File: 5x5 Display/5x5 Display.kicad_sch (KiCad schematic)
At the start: 46 parts, among them U3 DRV1

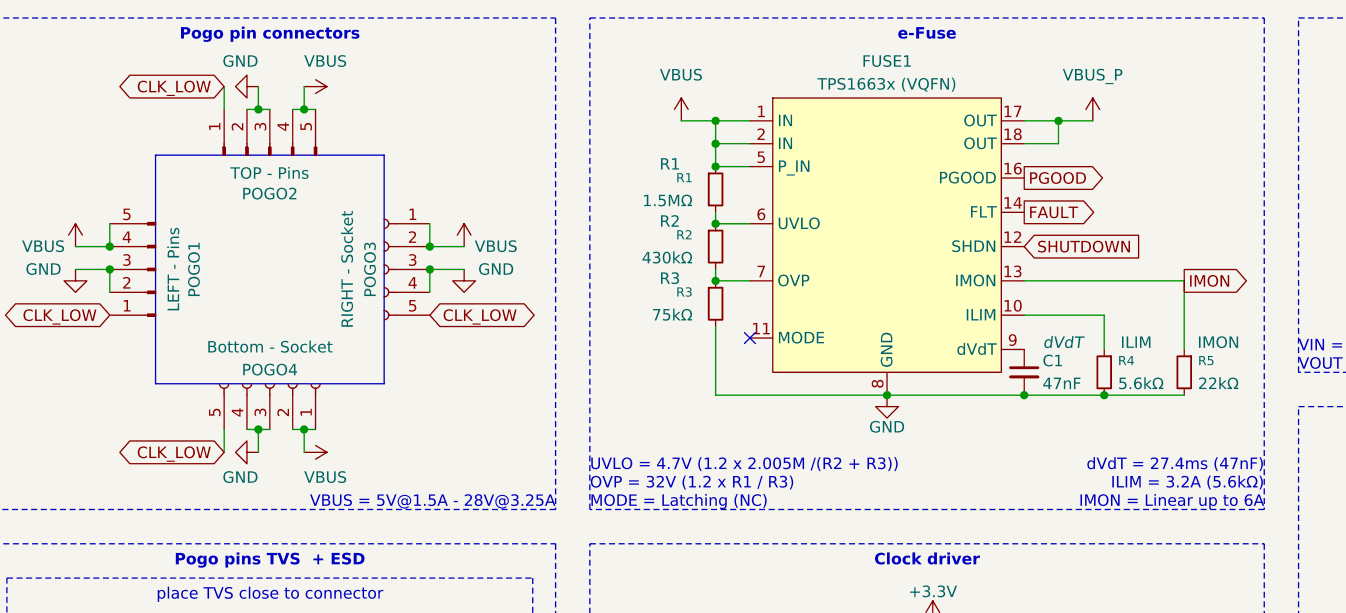
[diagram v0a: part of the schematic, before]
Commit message: Update schematic wiring and component positions
Adjusted wire routing and junctions around the 58.42mm y-coordinate, updated positions of R2 and R3, and changed some property values for clarity. These changes improve schematic readability and correct net connections in the 5x5 Display KiCad project.
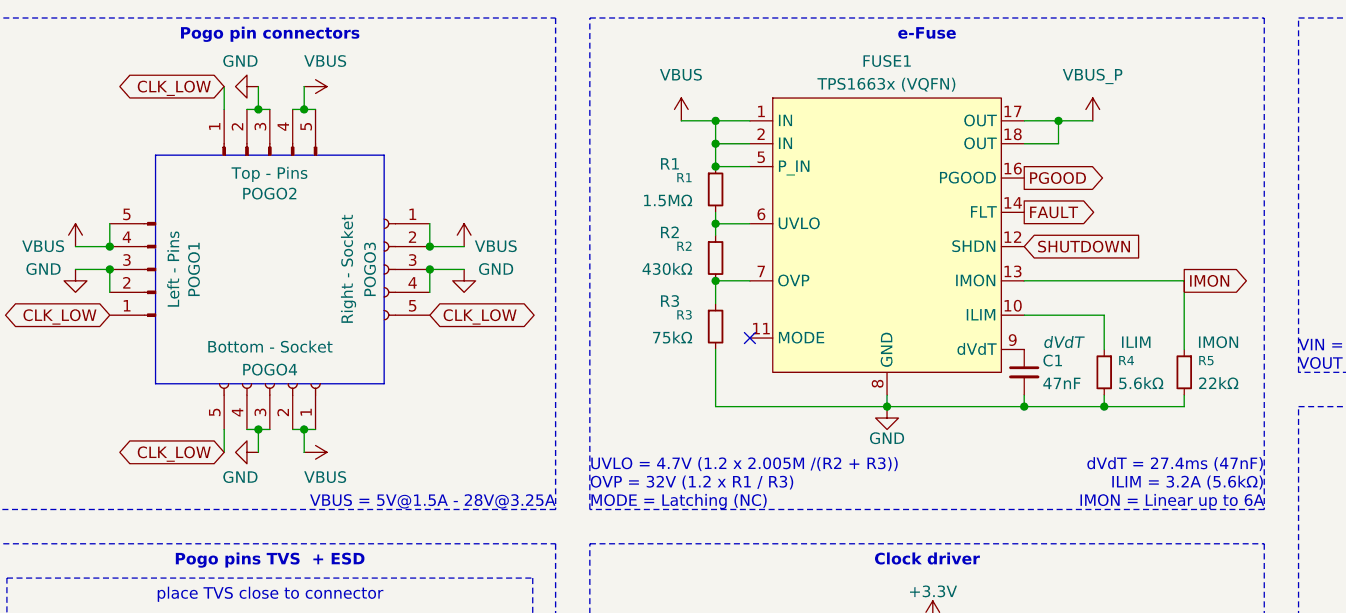
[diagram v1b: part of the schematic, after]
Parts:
- POGO1: value LEFT - Pins -> Left - Pins
- POGO2: value TOP - Pins -> Top - Pins
- POGO3: value RIGHT - Socket -> Right - Socket
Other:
- moved on the sheet: R2, R3
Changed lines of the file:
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@@
 	)
 	(junction
-		(at 250.19 100.33)
+		(at 130.81 58.42)
 		(diameter 0)
 		(color 0 0 0 0)
 	)
 	(junction
-		(at 218.44 80.01)
+		(at 250.19 100.33)
 		(diameter 0)
 		(color 0 0 0 0)
 	)
 	(junction
-		(at 208.28 74.93)
+		(at 218.44 80.01)
 		(diameter 0)
 		(color 0 0 0 0)
 	)
 	(junction
-		(at 96.52 38.1)
+		(at 208.28 74.93)
 		(diameter 0)
 		(color 0 0 0 0)
 	)
 	(junction
-		(at 139.7 57.15)
+		(at 96.52 38.1)
 		(diameter 0)
 		(color 0 0 0 0)
@@
 	)
 	(junction
-		(at 130.81 57.15)
+		(at 139.7 58.42)
 		(diameter 0)
 		(color 0 0 0 0)
@@
 	)
 	(junction
-		(at 115.57 57.15)
-		(diameter 0)
-		(color 0 0 0 0)
-	)
-	(junction
 		(at 171.45 69.85)
 		(diameter 0)
@@
 	)
 	(junction
+		(at 115.57 58.42)
+		(diameter 0)
+		(color 0 0 0 0)
+	)
+	(junction
 		(at 208.28 30.48)
 		(diameter 0)
@@
 	(wire
 		(pts
-			(xy 96.52 57.15) (xy 115.57 57.15)
+			(xy 96.52 46.99) (xy 96.52 44.45)
+		)
+		(stroke
+			(width 0)
+			(type default)
+		)
+	)
+	(wire
+		(pts
+			(xy 96.52 58.42) (xy 115.57 58.42)
 		)
 		(stroke
@@
 	(wire
 		(pts
+			(xy 96.52 39.37) (xy 96.52 38.1)
+		)
+		(stroke
+			(width 0)
+			(type default)
+		)
+	)
+	(wire
+		(pts
+			(xy 115.57 58.42) (xy 115.57 57.15)
+		)
+		(stroke
+			(width 0)
+			(type default)
+		)
+	)
+	(wire
+		(pts
 			(xy 64.77 40.64) (xy 64.77 38.1)
 		)
@@
 	(wire
 		(pts
-			(xy 115.57 57.15) (xy 130.81 57.15)
+			(xy 115.57 58.42) (xy 130.81 58.42)
 		)
 		(stroke
@@
 	(wire
 		(pts
+			(xy 139.7 58.42) (xy 139.7 57.15)
+		)
+		(stroke
+			(width 0)
+			(type default)
+		)
+	)
+	(wire
+		(pts
 			(xy 36.83 88.9) (xy 35.56 88.9)
 		)
@@
 	(wire
 		(pts
-			(xy 139.7 57.15) (xy 148.59 57.15)
+			(xy 139.7 58.42) (xy 148.59 58.42)
 		)
 		(stroke
@@
 	(wire
 		(pts
-			(xy 130.81 57.15) (xy 139.7 57.15)
+			(xy 130.81 58.42) (xy 139.7 58.42)
 		)
 		(stroke
@@
 	(wire
 		(pts
-			(xy 96.52 49.53) (xy 96.52 57.15)
-		)
-		(stroke
-			(width 0)
-			(type default)
-		)
-	)
-	(wire
-		(pts
-			(xy 96.52 43.18) (xy 96.52 44.45)
+			(xy 96.52 52.07) (xy 96.52 58.42)
 		)
 		(stroke
@@
 	(wire
 		(pts
+			(xy 130.81 58.42) (xy 130.81 57.15)
+		)
+		(stroke
+			(width 0)
+			(type default)
+		)
+	)
+	(wire
+		(pts
+			(xy 148.59 58.42) (xy 148.59 57.15)
+		)
+		(stroke
+			(width 0)
+			(type default)
+		)
+	)
+	(wire
+		(pts
 			(xy 96.52 36.83) (xy 96.52 38.1)
 		)
@@
 			)
 		)
-		(property "Value" "RIGHT - Socket"
+		(property "Value" "Right - Socket"
 			(at 55.626 43.18 90)
 			(effects
@@
 			)
 		)
-		(property "Value" "TOP - Pins"
+		(property "Value" "Top - Pins"
 			(at 46.99 32.512 90)
 			(effects
@@
 	(symbol
 		(lib_id "Device:R_Small")
-		(at 96.52 40.64 0)
+		(at 96.52 41.91 0)
 		(unit 1)
 		(exclude_from_sim no)
@@
 		(dnp no)
 		(property "Reference" "R2"
-			(at 93.98 39.3699 0)
+			(at 93.98 40.6399 0)
 			(effects
 				(font
@@
 		)
 		(property "Value" "430kΩ"
-			(at 93.98 41.9099 0)
+			(at 93.98 43.1799 0)
 			(effects
 				(font
@@
 		)
 		(property "Footprint" "Resistor_SMD:R_0603_1608Metric"
-			(at 96.52 40.64 0)
+			(at 96.52 41.91 0)
 			(effects
 				(font
@@
 		)
 		(property "Datasheet" "~"
-			(at 96.52 40.64 0)
+			(at 96.52 41.91 0)
 			(effects
 				(font
@@
 		)
 		(property "Description" "Resistor, small symbol"
-			(at 96.52 40.64 0)
+			(at 96.52 41.91 0)
 			(effects
 				(font
@@
 		)
 		(property "LCSC Part #" ""
-			(at 96.52 40.64 0)
+			(at 96.52 41.91 0)
 			(effects
 				(font
@@
 		)
 		(property "Name" "R2"
-			(at 91.44 37.846 0)
+			(at 91.44 39.116 0)
 			(effects
 				(font
@@
 	(symbol
 		(lib_id "power:GND")
-		(at 115.57 57.15 0)
+		(at 115.57 58.42 0)
 		(unit 1)
 		(exclude_from_sim no)
@@
 		(dnp no)
 		(property "Reference" "#PWR0161"
-			(at 115.57 63.5 0)
+			(at 115.57 64.77 0)
 			(effects
 				(font
@@
 		)
 		(property "Value" "GND"
-			(at 115.57 60.706 0)
+			(at 115.57 61.976 0)
 			(effects
 				(font
@@
 		)
 		(property "Footprint" ""
-			(at 115.57 57.15 0)
+			(at 115.57 58.42 0)
 			(effects
 				(font
@@
 		)
 		(property "Datasheet" ""
-			(at 115.57 57.15 0)
+			(at 115.57 58.42 0)
 			(effects
 				(font
@@
 		)
 		(property "Description" "Power symbol creates a global label with name \"GND\" , ground"
-			(at 115.57 57.15 0)
+			(at 115.57 58.42 0)
 			(effects
 				(font
@@
 	(symbol
 		(lib_id "Device:R_Small")
-		(at 96.52 46.99 0)
+		(at 96.52 49.53 0)
 		(unit 1)
 		(exclude_from_sim no)
@@
 		(dnp no)
 		(property "Reference" "R3"
-			(at 93.98 45.7199 0)
+			(at 93.98 48.2599 0)
 			(effects
 				(font
@@
 		)
 		(property "Value" "75kΩ"
-			(at 93.98 48.2599 0)
+			(at 93.98 50.7999 0)
 			(effects
 				(font
@@
 		)
 		(property "Footprint" "Resistor_SMD:R_0603_1608Metric"
-			(at 96.52 46.99 0)
+			(at 96.52 49.53 0)
 			(effects
 				(font
@@
 		)
 		(property "Datasheet" "~"
-			(at 96.52 46.99 0)
+			(at 96.52 49.53 0)
 			(effects
 				(font
@@
 		)
 		(property "Description" "Resistor, small symbol"
-			(at 96.52 46.99 0)
+			(at 96.52 49.53 0)
 			(effects
 				(font
@@
 		)
 		(property "LCSC Part #" ""
-			(at 96.52 46.99 0)
+			(at 96.52 49.53 0)
 			(effects
 				(font
@@
 		)
 		(property "Name" "R3"
-			(at 91.44 44.196 0)
+			(at 91.44 46.736 0)
 			(effects
 				(font
@@
 			)
 		)
-		(property "Value" "LEFT - Pins"
+		(property "Value" "Left - Pins"
 			(at 36.322 43.18 90)
 			(effects

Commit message: Footprint assignment finished
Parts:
- D10: footprint (none) -> Diode_SMD:D_SOD-323
- D6, D7, D8, D9: footprint (none) -> Diode_SMD:D_SMA
- L1, L2: footprint (none) -> Inductor_SMD:L_6.3x6.3_H3
- NT1, NT2: footprint (none) -> NetTie:NetTie-2_THT_Pad1.0mm
- POGO1, POGO2, POGO3, POGO4: footprint (none) -> Connector_PinSocket_2.54mm:PinSocket_1x05_P2.54mm_Horizontal
- REG1, REG2: footprint (none) -> TPS56637:TPS56637 VQFN-HR (10)
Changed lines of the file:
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@@
 			)
 		)
-		(property "Footprint" ""
+		(property "Footprint" "NetTie:NetTie-2_THT_Pad1.0mm"
 			(at 196.85 45.72 0)
 			(effects
@@
 			)
 		)
-		(property "Footprint" ""
+		(property "Footprint" "Diode_SMD:D_SMA"
 			(at 60.96 104.14 0)
 			(effects
@@
 			)
 		)
-		(property "Footprint" ""
+		(property "Footprint" "Diode_SMD:D_SMA"
 			(at 60.96 88.9 0)
 			(effects
@@
 			)
 		)
-		(property "Footprint" ""
+		(property "Footprint" "TPS56637:TPS56637 VQFN-HR (10)"
 			(at 195.58 76.2 0)
 			(effects
@@
 			)
 		)
-		(property "Footprint" ""
+		(property "Footprint" "TPS56637:TPS56637 VQFN-HR (10)"
 			(at 195.58 31.75 0)
 			(effects
@@
 			)
 		)
-		(property "Footprint" ""
+		(property "Footprint" "Connector_PinSocket_2.54mm:PinSocket_1x05_P2.54mm_Horizontal"
 			(at 59.69 43.18 0)
 			(effects
@@
 			)
 		)
-		(property "Footprint" ""
+		(property "Footprint" "Connector_PinSocket_2.54mm:PinSocket_1x05_P2.54mm_Horizontal"
 			(at 46.99 30.48 0)
 			(effects
@@
 			)
 		)
-		(property "Footprint" ""
+		(property "Footprint" "NetTie:NetTie-2_THT_Pad1.0mm"
 			(at 196.85 90.17 0)
 			(effects
@@
 			)
 		)
-		(property "Footprint" ""
+		(property "Footprint" "Diode_SMD:D_SOD-323"
 			(at 48.26 120.65 0)
 			(effects
@@
 			)
 		)
-		(property "Footprint" ""
+		(property "Footprint" "Diode_SMD:D_SMA"
 			(at 33.02 104.14 0)
 			(effects
@@
 			)
 		)
-		(property "Footprint" ""
+		(property "Footprint" "Connector_PinSocket_2.54mm:PinSocket_1x05_P2.54mm_Horizontal"
 			(at 46.99 55.88 0)
 			(effects
@@
 			)
 		)
-		(property "Footprint" ""
+		(property "Footprint" "Inductor_SMD:L_6.3x6.3_H3"
 			(at 212.09 74.93 0)
 			(effects
@@
 			)
 		)
-		(property "Footprint" ""
+		(property "Footprint" "Diode_SMD:D_SMA"
 			(at 33.02 88.9 0)
 			(effects
@@
 			)
 		)
-		(property "Footprint" ""
+		(property "Footprint" "Connector_PinSocket_2.54mm:PinSocket_1x05_P2.54mm_Horizontal"
 			(at 34.29 43.18 0)
 			(effects
@@
 			)
 		)
-		(property "Footprint" ""
+		(property "Footprint" "Inductor_SMD:L_6.3x6.3_H3"
 			(at 212.09 30.48 0)
 			(effects

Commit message: Add test points to schematic
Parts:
- added TP1: VBUS, symbol Connector:TestPoint
- added TP10, TP11, TP12: GND, symbol Connector:TestPoint
- added TP2: VBUS_P, symbol Connector:TestPoint
- added TP3: CLK_LOW, symbol Connector:TestPoint
- added TP4: CLK, symbol Connector:TestPoint
- added TP5: PGOOD, symbol Connector:TestPoint
- added TP6: +3.3v, symbol Connector:TestPoint
- added TP7: +5v, symbol Connector:TestPoint
- added TP8: LED LDO, symbol Connector:TestPoint
- added TP9: AGND, symbol Connector:TestPoint
- C1, C3, C6, C8, C9: footprint Capacitor_SMD:C_0805_2012Metric -> Capacitor_SMD:C_0603_1608Metric
- D10: now not fitted
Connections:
- net PGND is gone; now on net GND: C2.2, C5.2
- net +3.3V: now also TP6.1
- net +5V: now also TP7.1
- net +5V LED: now also TP8.1
- net AGND: now also TP9.1
- net CLK: now also TP4.1
- net CLK_LOW: now also TP3.1
- net GND: now also TP10.1, TP11.1, TP12.1
- net PGOOD: now also TP5.1
- net VBUS: now also TP1.1
- net VBUS_P: now also TP2.1
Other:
- note removed: "place TVS as close to connector as possible"
- moved on the sheet: D6, D7, D8, D9

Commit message: Assign test point footprints in schematic
Set the 'Footprint' property to 'TestPoint:TestPoint_Pad_D1.5mm' for multiple components in the 5x5 Display schematic. This change ensures correct footprint assignment for test points in PCB layout.
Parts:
- TP1, TP10, TP11, TP12, TP2, TP3, TP4, TP5, TP6, TP7, TP8, TP9: footprint (none) -> TestPoint:TestPoint_Pad_D1.5mm
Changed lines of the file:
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@@
 			)
 		)
-		(property "Footprint" ""
+		(property "Footprint" "TestPoint:TestPoint_Pad_D1.5mm"
 			(at 194.31 148.59 0)
 			(effects
@@
 			)
 		)
-		(property "Footprint" ""
+		(property "Footprint" "TestPoint:TestPoint_Pad_D1.5mm"
 			(at 167.64 148.59 0)
 			(effects
@@
 			)
 		)
-		(property "Footprint" ""
+		(property "Footprint" "TestPoint:TestPoint_Pad_D1.5mm"
 			(at 229.87 148.59 0)
 			(effects
@@
 			)
 		)
-		(property "Footprint" ""
+		(property "Footprint" "TestPoint:TestPoint_Pad_D1.5mm"
 			(at 265.43 148.59 0)
 			(effects
@@
 			)
 		)
-		(property "Footprint" ""
+		(property "Footprint" "TestPoint:TestPoint_Pad_D1.5mm"
 			(at 203.2 148.59 0)
 			(effects
@@
 			)
 		)
-		(property "Footprint" ""
+		(property "Footprint" "TestPoint:TestPoint_Pad_D1.5mm"
 			(at 185.42 148.59 0)
 			(effects
@@
 			)
 		)
-		(property "Footprint" ""
+		(property "Footprint" "TestPoint:TestPoint_Pad_D1.5mm"
 			(at 220.98 148.59 0)
 			(effects
@@
 			)
 		)
-		(property "Footprint" ""
+		(property "Footprint" "TestPoint:TestPoint_Pad_D1.5mm"
 			(at 238.76 148.59 0)
 			(effects
@@
 			)
 		)
-		(property "Footprint" ""
+		(property "Footprint" "TestPoint:TestPoint_Pad_D1.5mm"
 			(at 212.09 148.59 0)
 			(effects
@@
 			)
 		)
-		(property "Footprint" ""
+		(property "Footprint" "TestPoint:TestPoint_Pad_D1.5mm"
 			(at 247.65 148.59 0)
 			(effects
@@
 			)
 		)
-		(property "Footprint" ""
+		(property "Footprint" "TestPoint:TestPoint_Pad_D1.5mm"
 			(at 256.54 148.59 0)
 			(effects
@@
 			)
 		)
-		(property "Footprint" ""
+		(property "Footprint" "TestPoint:TestPoint_Pad_D1.5mm"
 			(at 176.53 148.59 0)
 			(effects

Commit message: buck layout
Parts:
- NT1, NT2: footprint NetTie:NetTie-2_THT_Pad1.0mm -> NetTie:NetTie-2_SMD_Pad0.5mm
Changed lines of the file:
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@@
 			)
 		)
-		(property "Footprint" "NetTie:NetTie-2_THT_Pad1.0mm"
+		(property "Footprint" "NetTie:NetTie-2_SMD_Pad0.5mm"
 			(at 196.85 45.72 0)
 			(effects
@@
 			)
 		)
-		(property "Footprint" "NetTie:NetTie-2_THT_Pad1.0mm"
+		(property "Footprint" "NetTie:NetTie-2_SMD_Pad0.5mm"
 			(at 196.85 90.17 0)
 			(effects

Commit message: Initial route complete
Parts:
- removed TP10, TP11: GND, TestPoint:TestPoint_Pad_D1.5mm, symbol Connector:TestPoint
- removed TP2: VBUS_P, TestPoint:TestPoint_Pad_D1.5mm, symbol Connector:TestPoint
- removed TP4: CLK, TestPoint:TestPoint_Pad_D1.5mm, symbol Connector:TestPoint
- removed TP5: PGOOD, TestPoint:TestPoint_Pad_D1.5mm, symbol Connector:TestPoint
- removed TP9: AGND, TestPoint:TestPoint_Pad_D1.5mm, symbol Connector:TestPoint
- D10: now left out of the parts list
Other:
- moved on the sheet: TP1, TP12, TP3, TP6, TP7, TP8

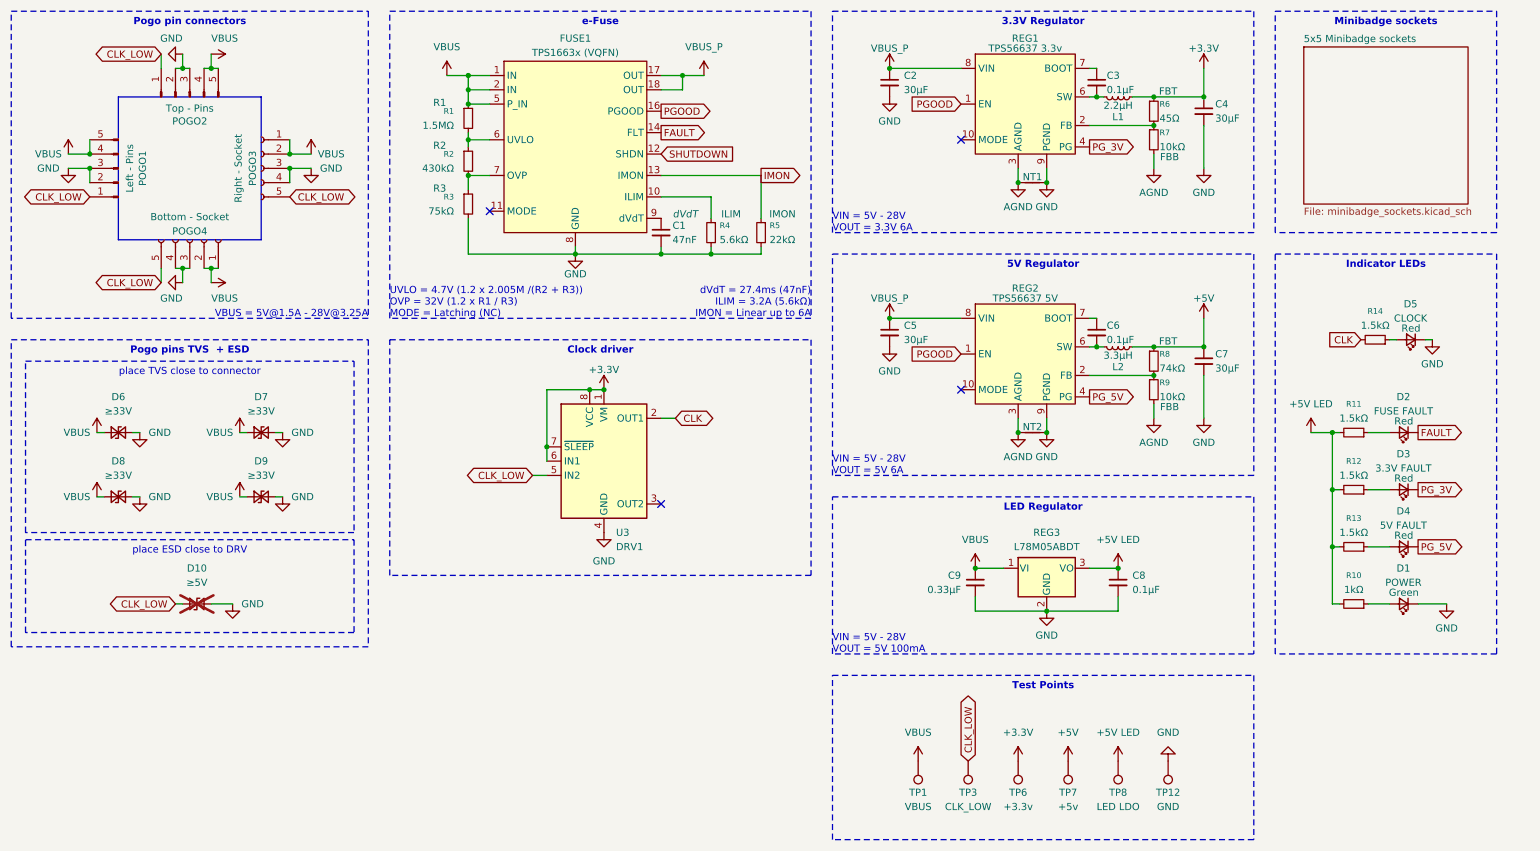
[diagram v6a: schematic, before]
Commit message: Silkscreens and components
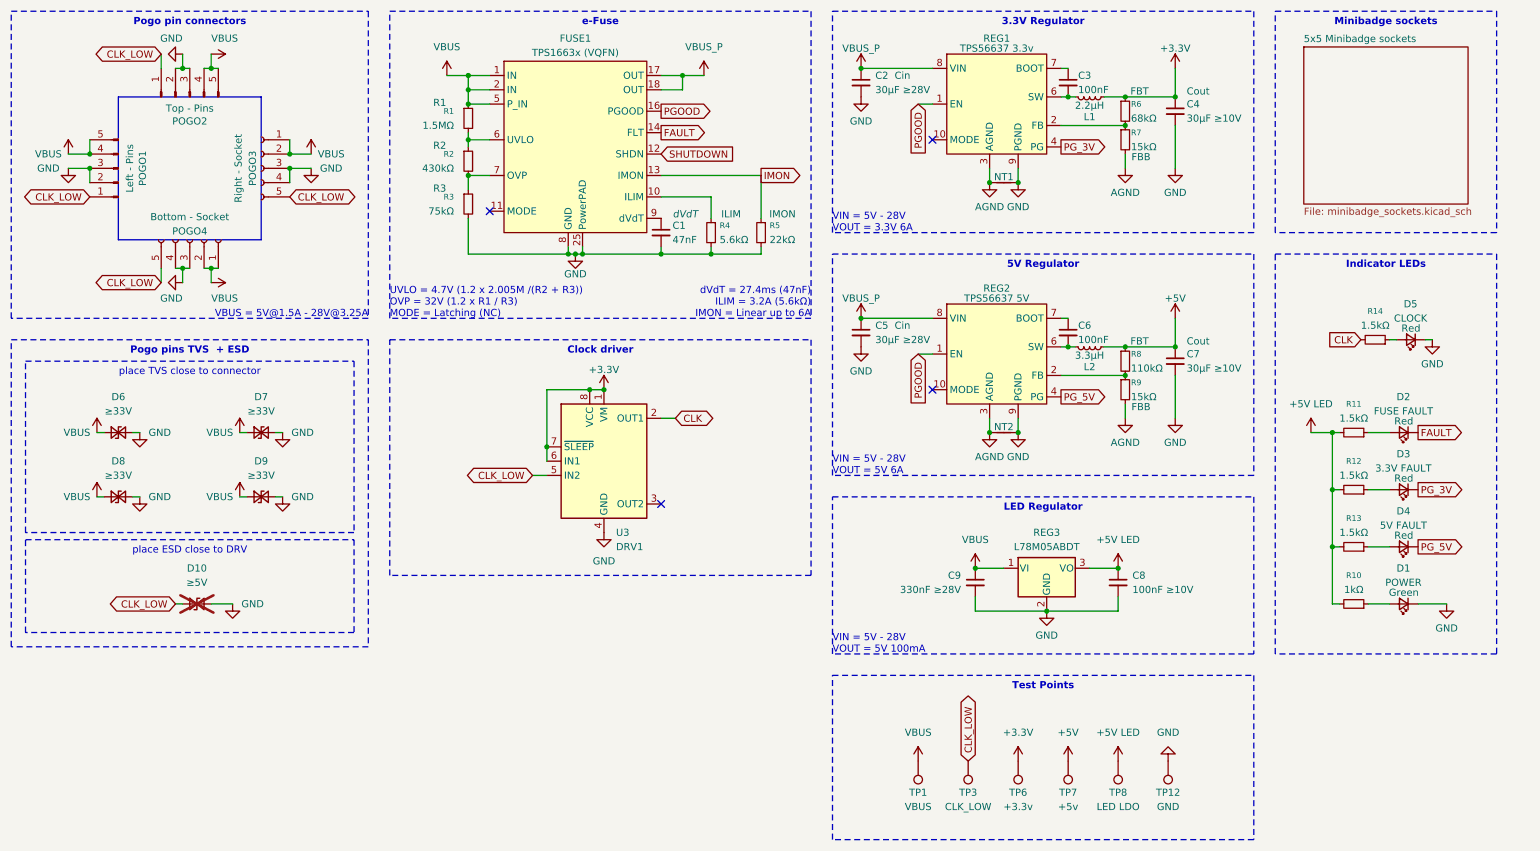
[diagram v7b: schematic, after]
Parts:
- C1: LCSC Part # (none) -> C1622
- C2, C5: value 30μF -> 30μF ≥28V; Name (none) -> Cin
- C3, C6: value 0.1μF -> 100nF; LCSC Part # (none) -> C14663
- C4, C7: value 30μF -> 30μF ≥10V; LCSC Part # (none) -> C96123; Name (none) -> Cout
- C8: value 0.1μF -> 100nF ≥10V; LCSC Part # (none) -> C14663
- C9: value 0.33μF -> 330nF ≥28V; footprint Capacitor_SMD:C_0603_1608Metric -> Capacitor_SMD:C_0805_2012Metric; LCSC Part # (none) -> C1740
- D1: LCSC Part # (none) -> C2297
- D2, D3, D4, D5: LCSC Part # (none) -> C84256
- R1: LCSC Part # (none) -> C4172
- R10: LCSC Part # (none) -> C21190
- R11, R12, R13, R14: LCSC Part # (none) -> C22843
- R2: LCSC Part # (none) -> C25969
- R3: LCSC Part # (none) -> C23242
- R4: LCSC Part # (none) -> C23189
- R5: LCSC Part # (none) -> C31850
- R6: value 45Ω -> 68kΩ; LCSC Part # (none) -> C23231
- R7, R9: value 10kΩ -> 15kΩ; LCSC Part # (none) -> C22809
- R8: value 74kΩ -> 110kΩ; LCSC Part # (none) -> C25805
- TP1, TP12, TP3, TP6, TP7, TP8: now left out of the parts list
- U3: LCSC Part # (none) -> C191000
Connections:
- net GND: now also FUSE1.25 (PowerPAD)
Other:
- moved on the sheet: C2, C3, C4, C5, C6, C7, L1, L2, NT1, NT2, R6, R7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
